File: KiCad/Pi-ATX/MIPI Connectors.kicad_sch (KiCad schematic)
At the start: 2 parts, among them J1 DVI-D_Dual_Link, J2 DVI-D_Dual_Link

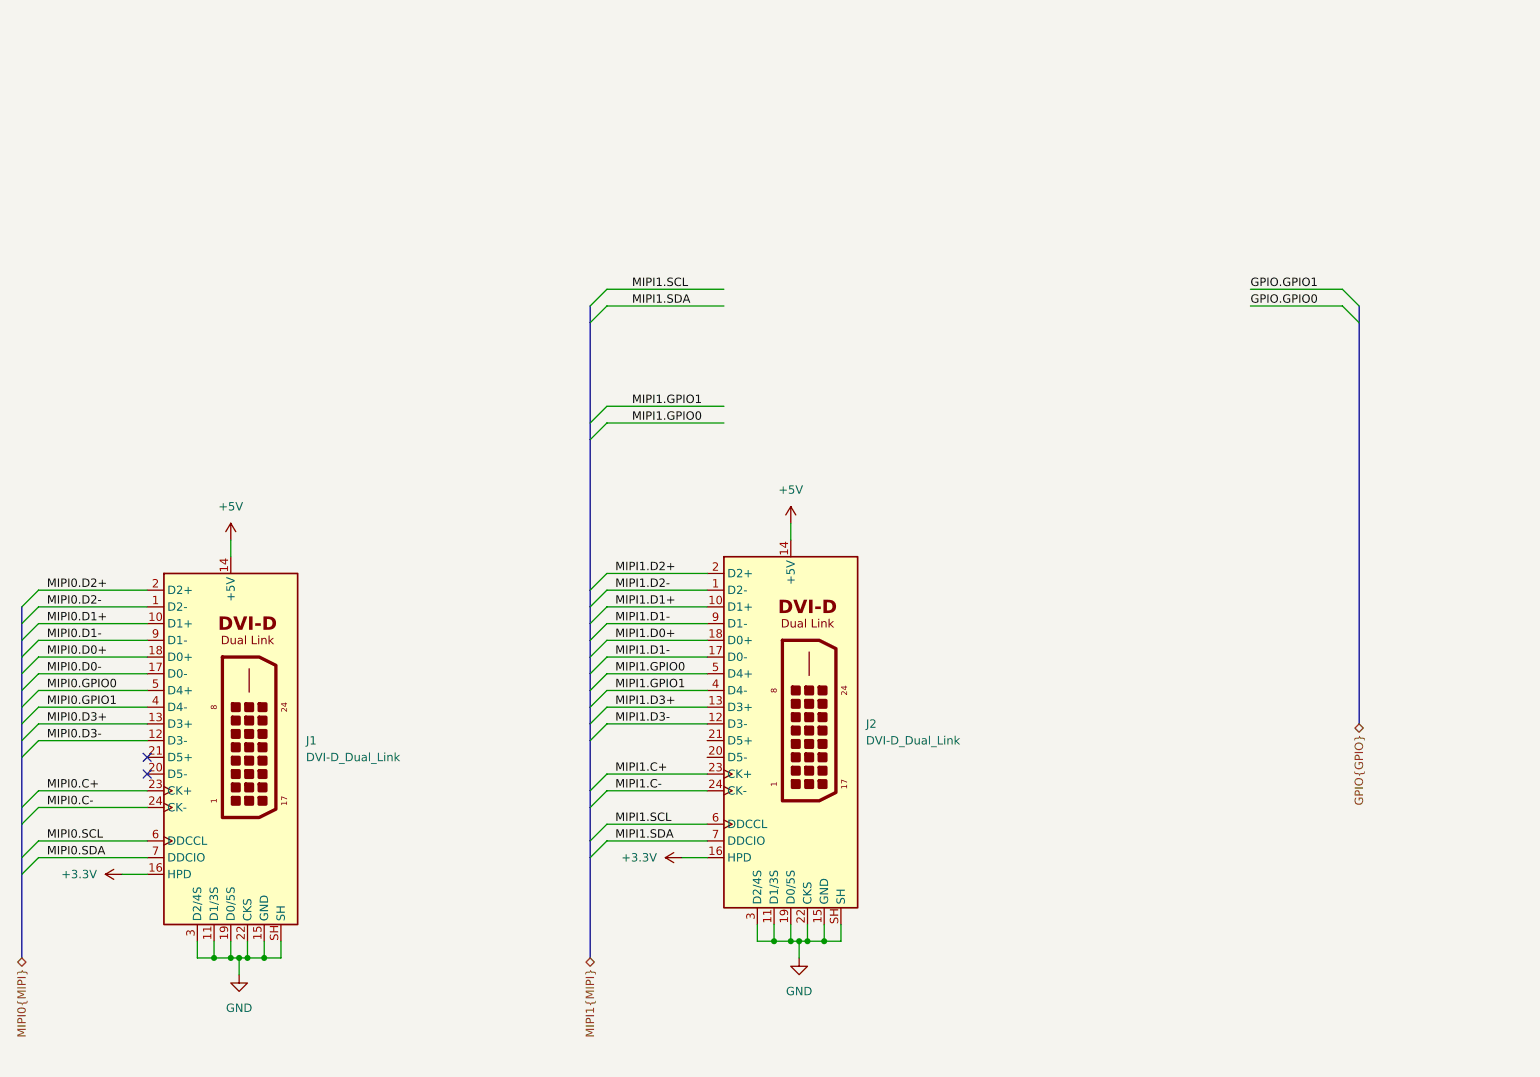
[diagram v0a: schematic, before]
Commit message: Finished MIPI Connector Schematic
-finished MIPI connector schematic page
-updated CM5 symbol to v0.2 version from my RPI CM library
-updated to do list
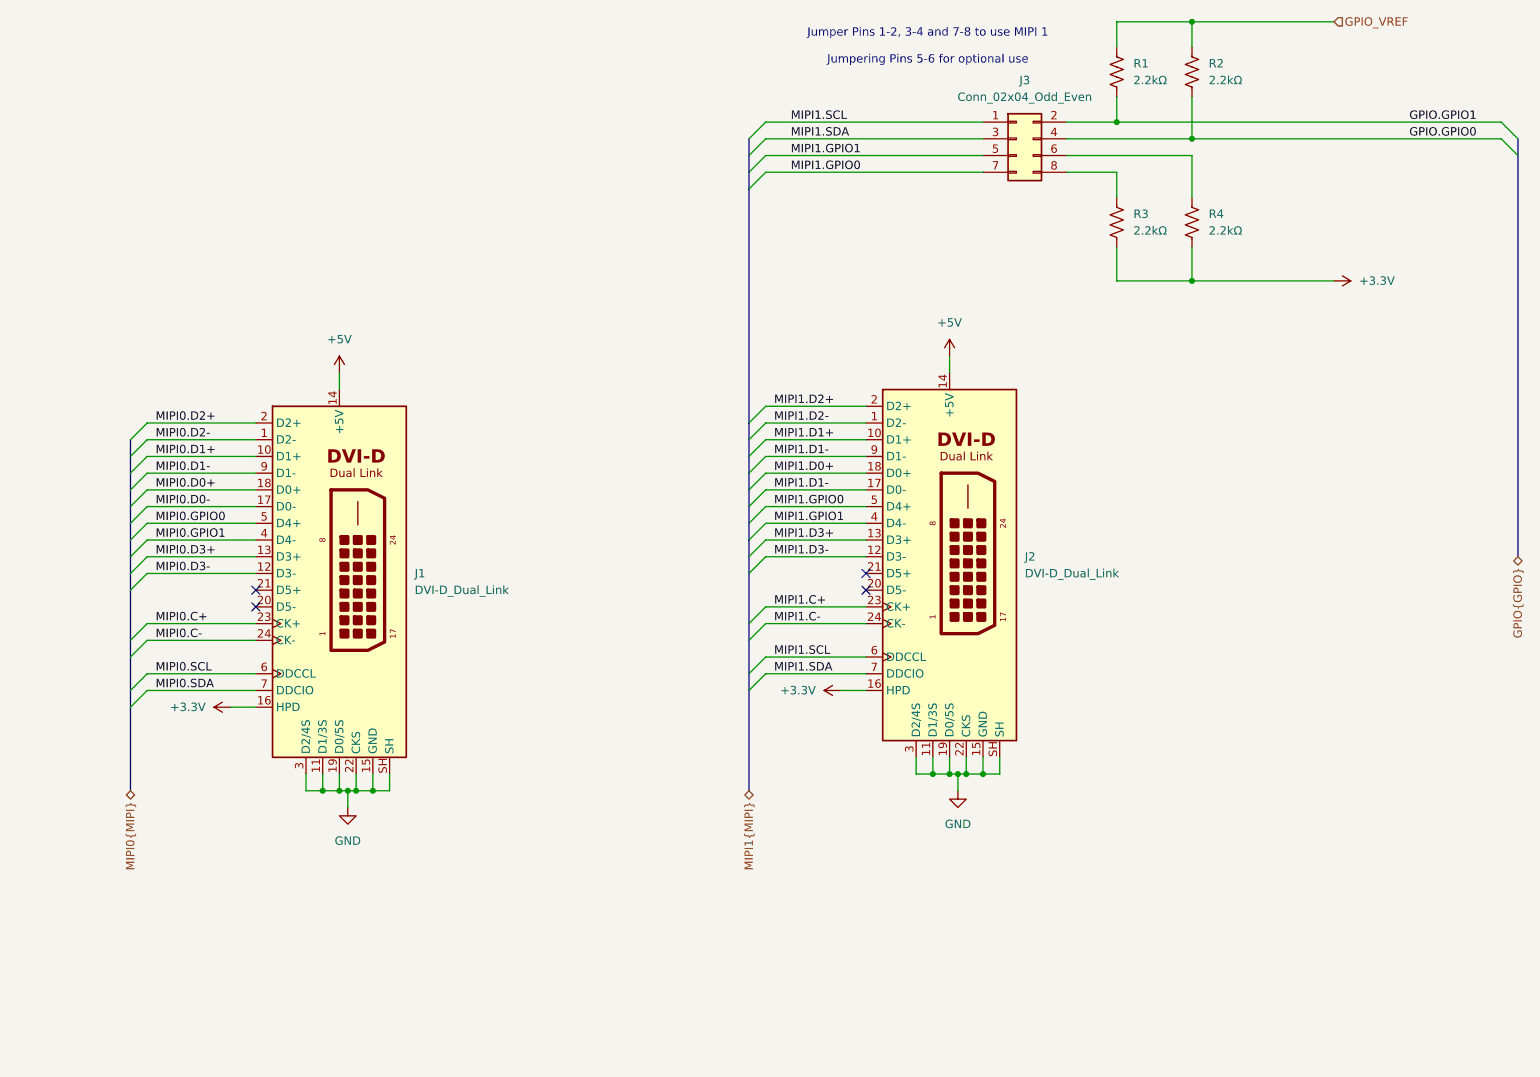
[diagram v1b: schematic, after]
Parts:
- added J3: Conn_02x04_Odd_Even, Connector_PinHeader_2.54mm:PinHeader_2x04_P2.54mm_Vertical, symbol Connector_Generic:Conn_02x04_Odd_Even
- added R1, R2, R3, R4: 2.2kΩ, Resistor_SMD:R_0402_1005Metric, symbol Device:R_US
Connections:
- net +3.3V: now also R3.2, R4.2
- net GPIO.GPIO0: now also J3.4 (Pin_4), R2.2
- net GPIO.GPIO1: now also J3.2 (Pin_2), R1.2
- net MIPI1.GPIO0: now also J3.7 (Pin_7)
- net MIPI1.GPIO1: now also J3.5 (Pin_5)
- net MIPI1.SCL: now also J3.1 (Pin_1)
- net MIPI1.SDA: now also J3.3 (Pin_3)
- new net: J3.6 (Pin_6), R4.1
- new net: J3.8 (Pin_8), R3.1
- new net GPIO_VREF: R1.1, R2.1
- no-connect marks 2 -> 4
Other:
- note added: "Jumper Pins 1-2, 3-4 and 7-8 to use MIPI 1 Jumpering Pins 5-6 for optional use"
- moved on the sheet: J1, J2
